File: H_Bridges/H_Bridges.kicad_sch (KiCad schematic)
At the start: 25 parts, among them Q1 IRF540NSTRLPBF, Q2 IRF540NSTRLPBF, Q3 IRF540NSTRLPBF, Q4 IRF540NSTRLPBF, Q5 IRF540NSTRLPBF, Q6 IRF540NSTRLPBF, Q7 IRF540NSTRLPBF, Q8 IRF540NSTRLPBF

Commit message: added connector
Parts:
- added J1: S4B-PH-K-SLFSN, CONN_S4B-PH-K-S_JST, symbol S4B_PH_K_S_LF__SN_:S4B-PH-K-SLFSN
- added U1: ESP8266, symbol Detection_Eval_lib:ESP_Hold
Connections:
- net Coil_A-: now also J1.1, J1.2, J1.3, J1.4
- net GND: now also U1.10 (GND), U1.11 (GND_usb)
- net P1: now also U1.4 (GPIO16)
- net P2: now also U1.5 (GPIO14)
- net P3: now also U1.6 (GPIO12)
- net P4: now also U1.7 (GPIO13)
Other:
- moved on the sheet: D5

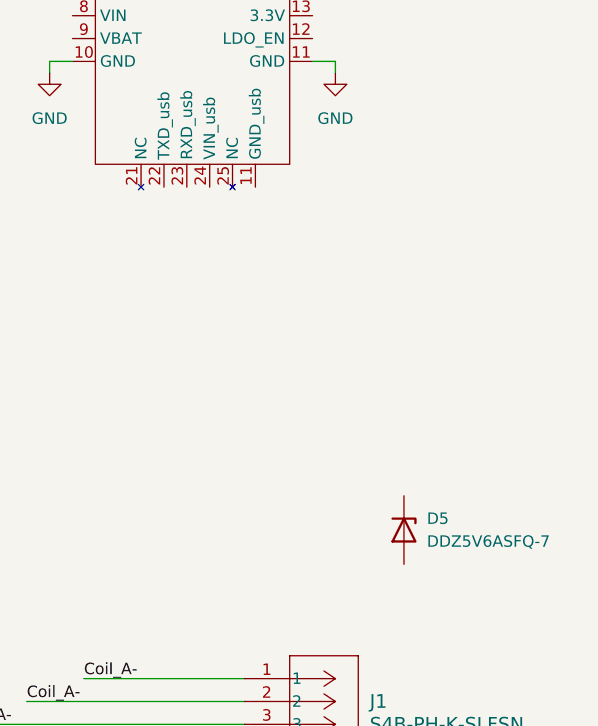
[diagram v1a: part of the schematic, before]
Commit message: created footprint for ESP
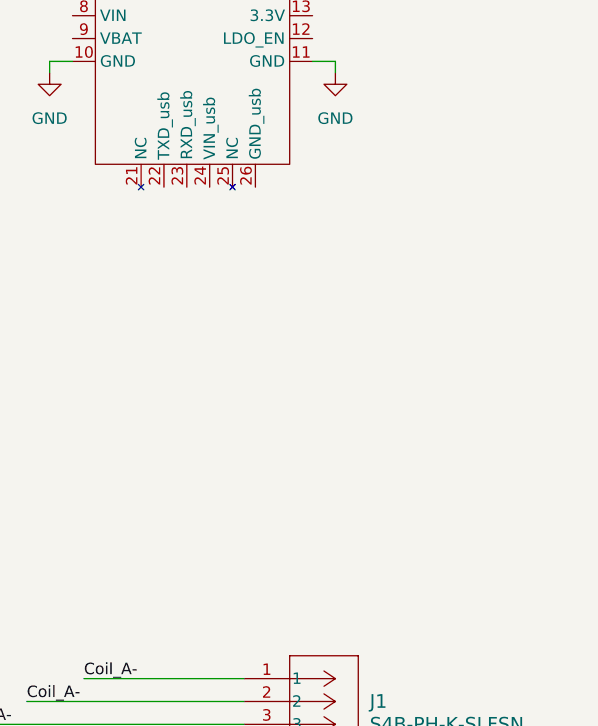
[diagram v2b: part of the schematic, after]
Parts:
- removed D5: DDZ5V6ASFQ-7, Footprints:DDZ5V6ASFQ-7_DIO, symbol Device:D_Zener
- U1: footprint (none) -> ESP8266_THT:ESP8266_THT
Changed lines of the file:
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@@
-	)
-	(symbol
-		(lib_id "Device:D_Zener")
-		(at 256.54 102.87 270)
-		(unit 1)
-		(exclude_from_sim no)
-		(in_bom yes)
-		(on_board yes)
-		(dnp no)
-		(fields_autoplaced yes)
-		(property "Reference" "D5"
-			(at 259.08 101.5999 90)
-			(effects
-				(font
-					(size 1.27 1.27)
-				)
-				(justify left)
-			)
-		)
-		(property "Value" "DDZ5V6ASFQ-7"
-			(at 259.08 104.1399 90)
-			(effects
-				(font
-					(size 1.27 1.27)
-				)
-				(justify left)
-			)
-		)
-		(property "Footprint" "Footprints:DDZ5V6ASFQ-7_DIO"
-			(at 256.54 102.87 0)
-			(effects
-				(font
-					(size 1.27 1.27)
-				)
-				(hide yes)
-			)
-		)
-		(property "Datasheet" "~"
-			(at 256.54 102.87 0)
-			(effects
-				(font
-					(size 1.27 1.27)
-				)
-				(hide yes)
-			)
-		)
-		(property "Description" "Zener diode"
-			(at 256.54 102.87 0)
-			(effects
-				(font
-					(size 1.27 1.27)
-				)
-				(hide yes)
-			)
-		)
-		(pin "1"
-		)
-		(pin "2"
-		)
-		(instances
-			(project "H_Bridges"
-				(path "/a020a591-cea5-4f16-9764-82374c05e734"
-					(reference "D5")
-					(unit 1)
-				)
-			)
-		)
 	)
 	(symbol
@@
 			)
 		)
-		(property "Footprint" ""
+		(property "Footprint" "ESP8266_THT:ESP8266_THT"
 			(at 229.87 49.53 0)
 			(effects
@@
 		(pin "19"
 		)
-		(pin "11"
+		(pin "26"
 		)
 		(pin "6"

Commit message: added 0 ohms
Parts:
- added R10, R9: 0, symbol Device:R_US
- J1: footprint CONN_S4B-PH-K-S_JST -> Footprints:CONN_S4B-PH-K-S_JST
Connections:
- net Coil_A+: now also J1.1
- net Coil_A-: no longer J1.1, J1.2, J1.4
- net Coil_B+: now also J1.4
- net Coil_B-: now also J1.2
- net at U1.8 (VIN): now also R9.1
- net at U1.9 (VBAT): now also R10.1
- new net +3V0: R10.2, R9.2
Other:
- moved on the sheet: J1

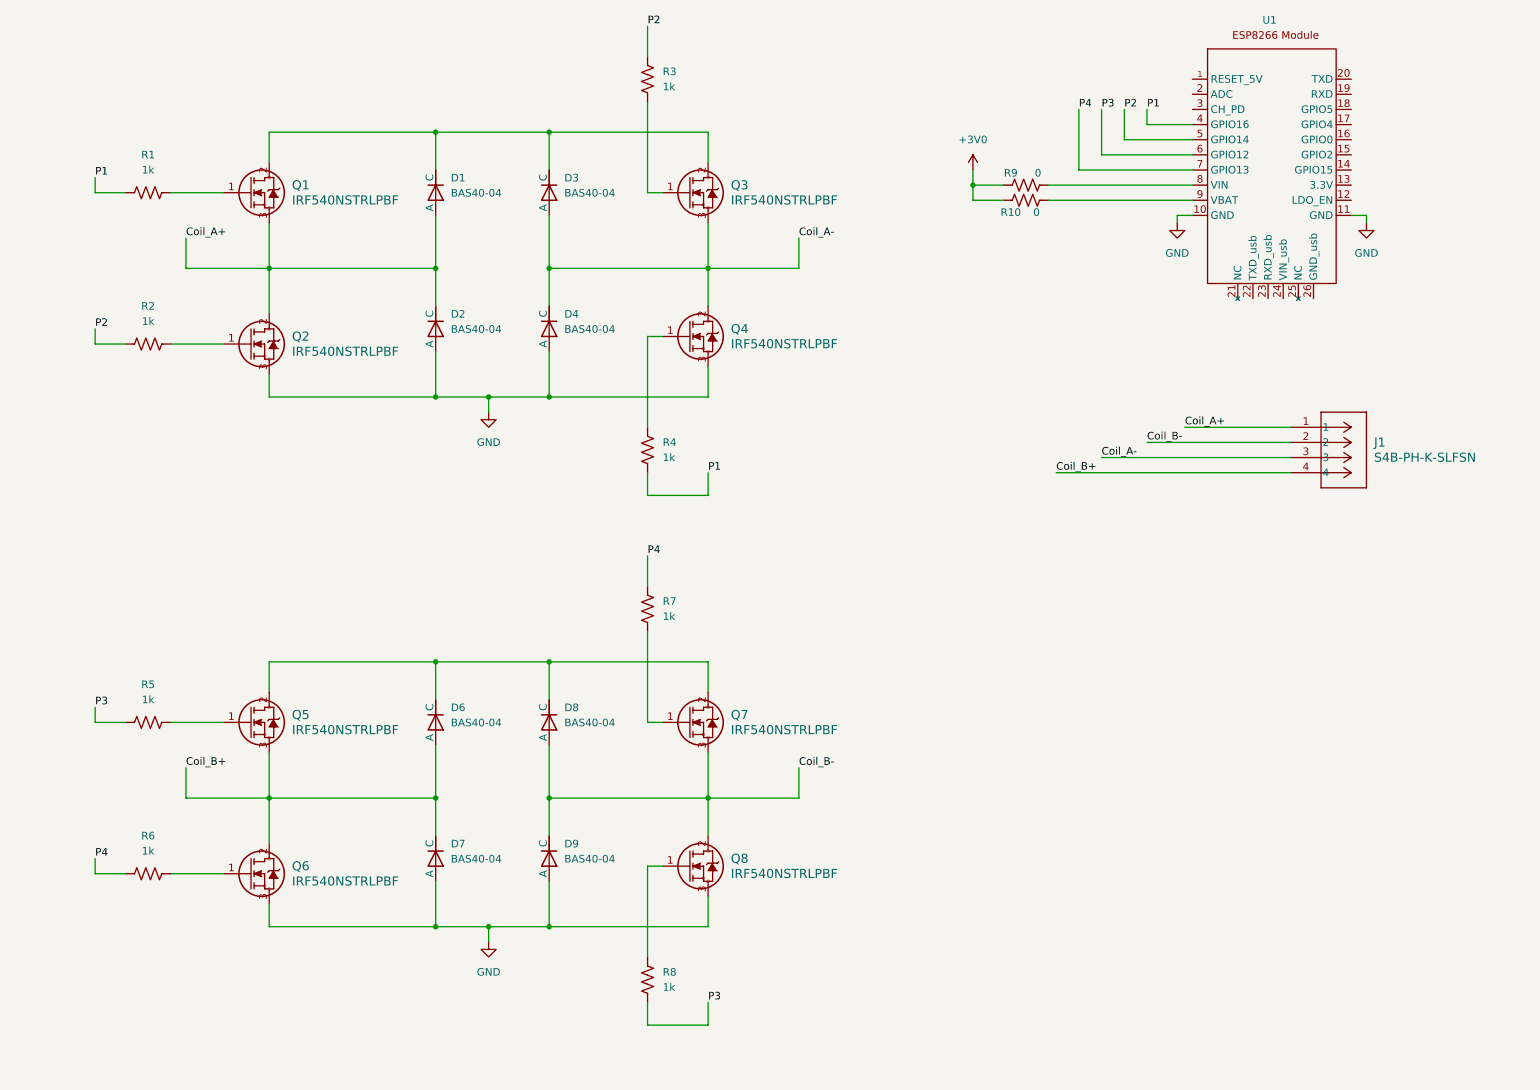
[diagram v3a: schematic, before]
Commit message: added battery + sym/foot
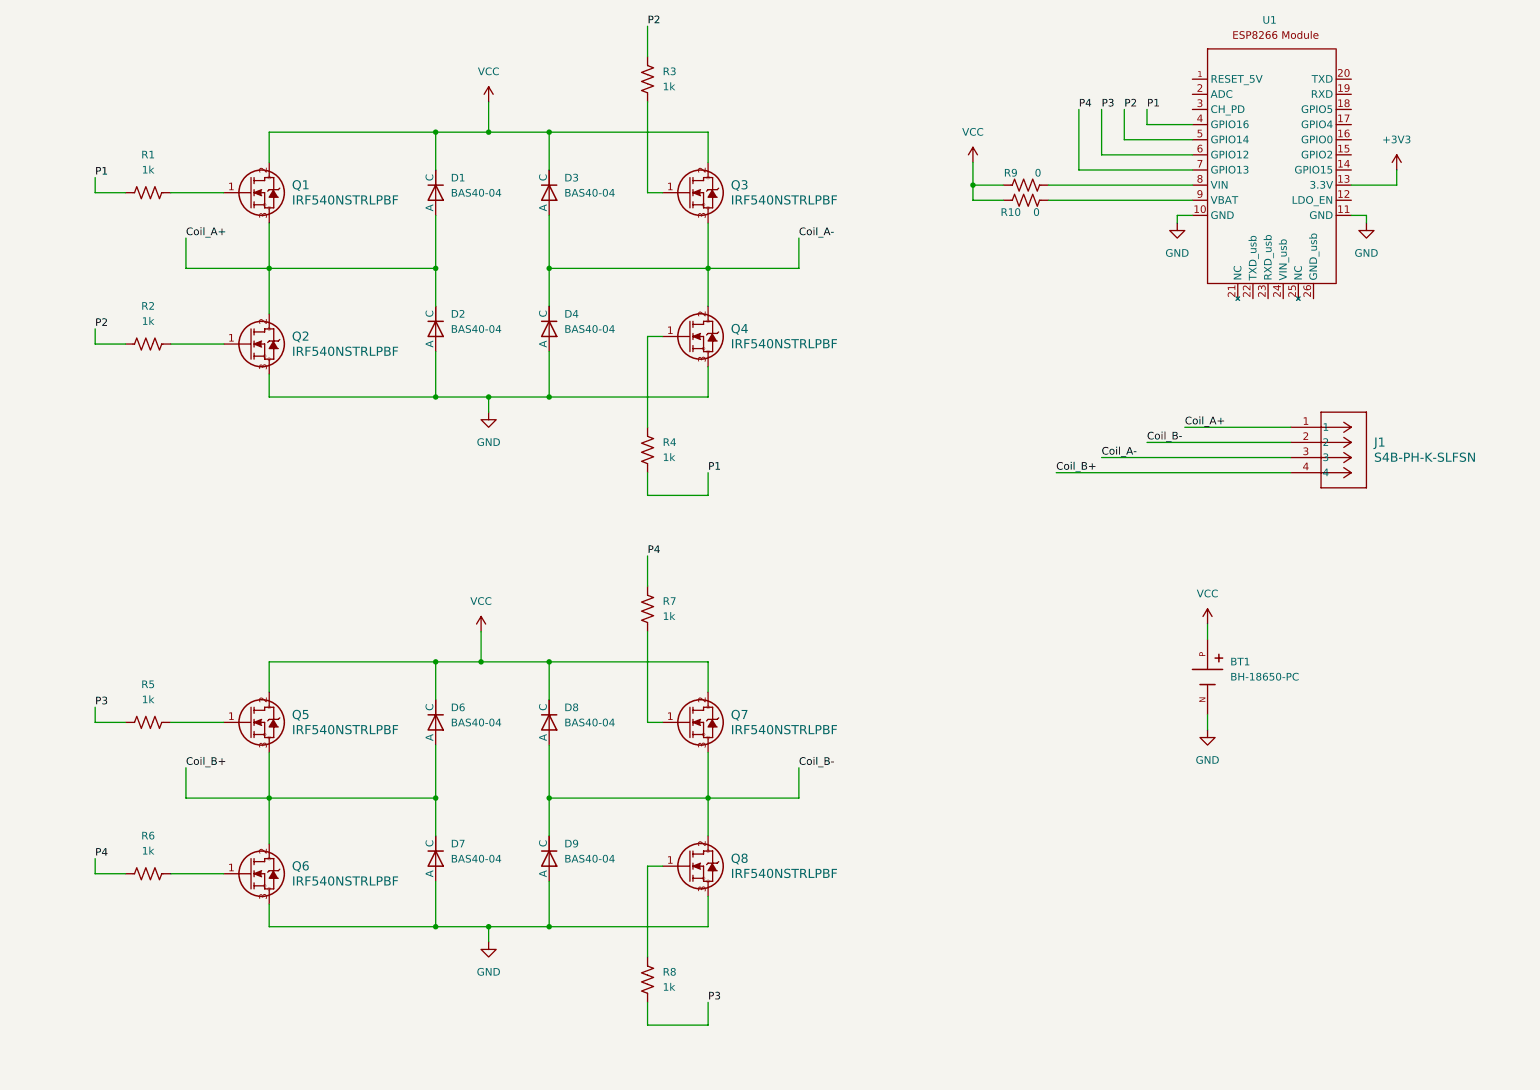
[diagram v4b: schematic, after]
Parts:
- added BT1: BH-18650-PC, BH-18650-PC:BAT_BH-18650-PC, symbol BH-18650-PC:BH-18650-PC
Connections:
- net +3V0 is gone; now on net VCC: R10.2, R9.2
- net GND: now also BT1.N
- net VCC: now reaches D6.2 (C), D8.2 (C), Q5.2, Q7.2
- net VCC: now also D1.2 (C), D3.2 (C), Q1.2, Q3.2, BT1.P
- net +3V3: now reaches U1.13 (3.3V)

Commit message: started charge circuit
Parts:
- BT1: footprint BH-18650-PC:BAT_BH-18650-PC -> Footprints:BAT_BH-18650-PC
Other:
- added sheet Charger (chargecircuit.kicad_sch)
- moved on the sheet: BT1, D1, D2, D3, D4, D6, D7, D8, D9, Q1, Q2, Q3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

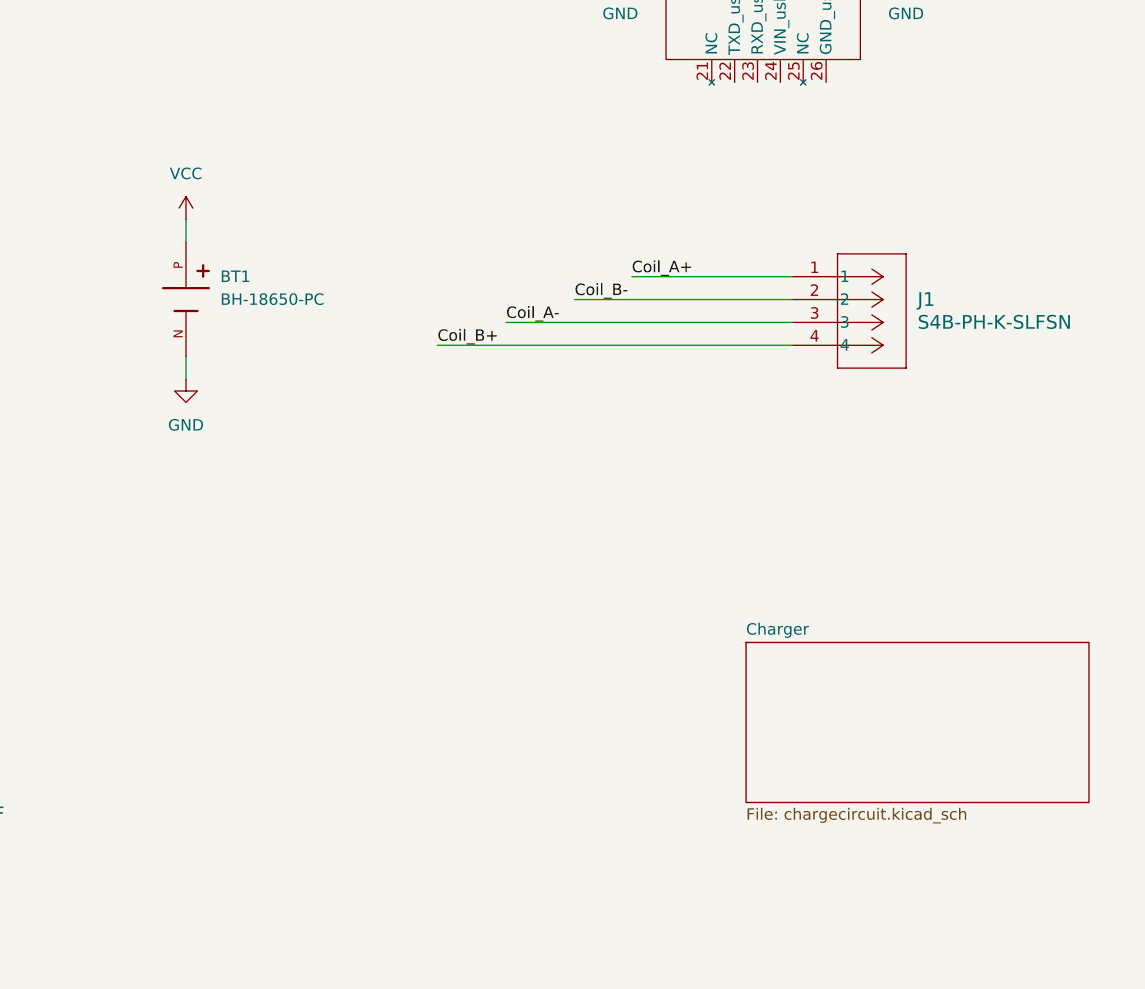
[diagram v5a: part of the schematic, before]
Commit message: USB-C Input and Isolation Circuit
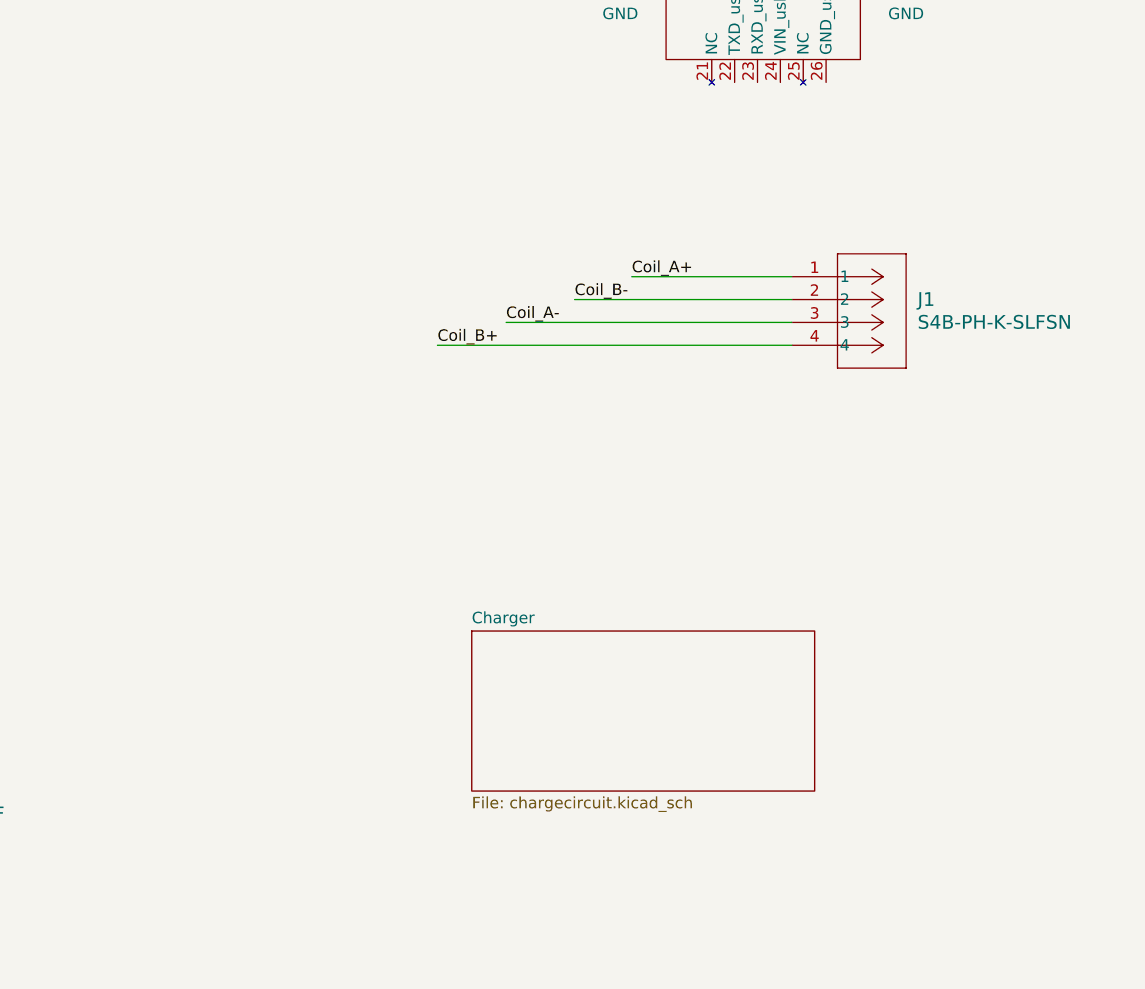
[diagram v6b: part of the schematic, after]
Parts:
- removed BT1: BH-18650-PC, Footprints:BAT_BH-18650-PC, symbol BH-18650-PC:BH-18650-PC
